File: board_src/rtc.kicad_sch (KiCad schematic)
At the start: 8 parts, among them IC1 PCF8563TS_4,118, J9 Conn_01x02_Pin, Y2 Crystal

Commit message: wersja dodane arkusze hierarchiczne
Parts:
- removed BT1: Battery, symbol Device:Battery
- added BT2: 502-3, 5023, symbol 502-3:502-3
- added R17, R18: 10k, Resistor_SMD:R_0201_0603Metric, symbol Device:R
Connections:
- net +3.3V is gone; now on net 3,3V: IC1.8 (VDD)
- net SCL: now also R17.1
- net SDA: now also R18.1
- net at D13.2 (A): now also BT2.2 (+)
- net 3,3V: now reaches D12.2 (A)
- net 3,3V: now also R17.2, R18.2
- net GND renamed gnd
- net gnd: now also BT2.1 (-)
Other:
- note removed: "Jakich elementów brakuje?"
- moved on the sheet: C1, C2, D12, D13, IC1, J9, Y2

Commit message: wersja dodane arkusze hierarchiczne
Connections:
- net 3,3V renamed +3.3V
- net gnd renamed GND
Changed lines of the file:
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@@
-	(wire
-		(pts
-			(xy 162.56 127) (xy 160.02 127)
-		)
-		(stroke
-			(width 0)
-			(type default)
-		)
-	)
 	(wire
 		(pts
@@
 		)
 	)
-	(global_label "3,3V"
-		(shape input)
-		(at 242.57 81.28 0)
-		(fields_autoplaced yes)
-		(effects
-			(font
-				(size 1.27 1.27)
-			)
-			(justify left)
-		)
-		(property "Intersheetrefs" "${INTERSHEET_REFS}"
-			(at 249.6676 81.28 0)
-			(effects
-				(font
-					(size 1.27 1.27)
-				)
-				(justify left)
-				(hide yes)
-			)
-		)
-	)
-	(global_label "3,3V"
-		(shape input)
-		(at 114.3 59.69 0)
-		(fields_autoplaced yes)
-		(effects
-			(font
-				(size 1.27 1.27)
-			)
-			(justify left)
-		)
-		(property "Intersheetrefs" "${INTERSHEET_REFS}"
-			(at 121.3976 59.69 0)
-			(effects
-				(font
-					(size 1.27 1.27)
-				)
-				(justify left)
-				(hide yes)
-			)
-		)
-	)
-	(global_label "gnd"
-		(shape input)
-		(at 160.02 127 180)
-		(fields_autoplaced yes)
-		(effects
-			(font
-				(size 1.27 1.27)
-			)
-			(justify right)
-		)
-		(property "Intersheetrefs" "${INTERSHEET_REFS}"
-			(at 153.5878 127 0)
-			(effects
-				(font
-					(size 1.27 1.27)
-				)
-				(justify right)
-				(hide yes)
-			)
-		)
-	)
 	(symbol
 		(lib_id "Device:R")
@@
 	)
 	(symbol
+		(lib_id "power:GND")
+		(at 162.56 127 0)
+		(unit 1)
+		(exclude_from_sim no)
+		(in_bom yes)
+		(on_board yes)
+		(dnp no)
+		(fields_autoplaced yes)
+		(property "Reference" "#PWR018"
+			(at 162.56 133.35 0)
+			(effects
+				(font
+					(size 1.27 1.27)
+				)
+				(hide yes)
+			)
+		)
+		(property "Value" "GND"
+			(at 162.56 132.08 0)
+			(effects
+				(font
+					(size 1.27 1.27)
+				)
+			)
+		)
+		(property "Footprint" ""
+			(at 162.56 127 0)
+			(effects
+				(font
+					(size 1.27 1.27)
+				)
+				(hide yes)
+			)
+		)
+		(property "Datasheet" ""
+			(at 162.56 127 0)
+			(effects
+				(font
+					(size 1.27 1.27)
+				)
+				(hide yes)
+			)
+		)
+		(property "Description" "Power symbol creates a global label with name \"GND\" , ground"
+			(at 162.56 127 0)
+			(effects
+				(font
+					(size 1.27 1.27)
+				)
+				(hide yes)
+			)
+		)
+		(pin "1"
+		)
+		(instances
+			(project ""
+				(path "/772e9f49-cfcf-4cf6-843d-0684684f2d4b/aeaae9df-f534-49c0-80c6-5a1da97c1479"
+					(reference "#PWR018")
+					(unit 1)
+				)
+			)
+		)
+	)
+	(symbol
 		(lib_id "Device:C")
 		(at 127 80.01 180)
@@
 					(unit 1)
 				)
+			)
+		)
+	)
+	(symbol
+		(lib_id "power:+3.3V")
+		(at 114.3 59.69 270)
+		(unit 1)
+		(exclude_from_sim no)
+		(in_bom yes)
+		(on_board yes)
+		(dnp no)
+		(fields_autoplaced yes)
+		(property "Reference" "#PWR019"
+			(at 110.49 59.69 0)
+			(effects
+				(font
+					(size 1.27 1.27)
+				)
+				(hide yes)
+			)
+		)
+		(property "Value" "+3.3V"
+			(at 118.11 59.6899 90)
+			(effects
+				(font
+					(size 1.27 1.27)
+				)
+				(justify left)
+			)
+		)
+		(property "Footprint" ""
+			(at 114.3 59.69 0)
+			(effects
+				(font
+					(size 1.27 1.27)
+				)
+				(hide yes)
+			)
+		)
+		(property "Datasheet" ""
+			(at 114.3 59.69 0)
+			(effects
+				(font
+					(size 1.27 1.27)
+				)
+				(hide yes)
+			)
+		)
+		(property "Description" "Power symbol creates a global label with name \"+3.3V\""
+			(at 114.3 59.69 0)
+			(effects
+				(font
+					(size 1.27 1.27)
+				)
+				(hide yes)
+			)
+		)
+		(pin "1"
+		)
+		(instances
+			(project "board"
+				(path "/772e9f49-cfcf-4cf6-843d-0684684f2d4b/aeaae9df-f534-49c0-80c6-5a1da97c1479"
+					(reference "#PWR019")
+					(unit 1)
+				)
+			)
+		)
+	)
+	(symbol
+		(lib_id "power:+3.3V")
+		(at 242.57 81.28 270)
+		(unit 1)
+		(exclude_from_sim no)
+		(in_bom yes)
+		(on_board yes)
+		(dnp no)
+		(fields_autoplaced yes)
+		(property "Reference" "#PWR011"
+			(at 238.76 81.28 0)
+			(effects
+				(font
+					(size 1.27 1.27)
+				)
+				(hide yes)
+			)
+		)
+		(property "Value" "+3.3V"
+			(at 246.38 81.2799 90)
+			(effects
+				(font
+					(size 1.27 1.27)
+				)
+				(justify left)
+			)
+		)
+		(property "Footprint" ""
+			(at 242.57 81.28 0)
+			(effects
+				(font
+					(size 1.27 1.27)
+				)
+				(hide yes)
+			)
+		)
+		(property "Datasheet" ""
+			(at 242.57 81.28 0)
+			(effects
+				(font
+					(size 1.27 1.27)
+				)
+				(hide yes)
+			)
+		)
+		(property "Description" "Power symbol creates a global label with name \"+3.3V\""
+			(at 242.57 81.28 0)
+			(effects
+				(font
+					(size 1.27 1.27)
+				)
+				(hide yes)
+			)
+		)
+		(pin "1"
+		)
+		(instances
+			(project "board"
+				(path "/772e9f49-cfcf-4cf6-843d-0684684f2d4b/aeaae9df-f534-49c0-80c6-5a1da97c1479"
+					(reference "#PWR011")
+					(unit 1)
+				)

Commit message: wersja uzupelnione footprinty
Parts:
- BT2: footprint 5023 -> footprints:podstawka_bateria
- IC1: footprint SOP65P490X110-8N -> footprints:SOP65P490X110-8N
- J9: footprint (none) -> Connector_PinHeader_2.54mm:PinHeader_1x02_P2.54mm_Vertical
- Y2: footprint (none) -> Crystal:Crystal_HC35-U
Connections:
- net SCL: no longer names the net of IC1.6 (SCL), R17.1
- net SDA: no longer names the net of IC1.5 (SDA), R18.1
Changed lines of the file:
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@@
-		)
-	)
-	(label "SDA"
-		(at 220.98 82.55 0)
-		(effects
-			(font
-				(size 1.27 1.27)
-			)
-			(justify left bottom)
-		)
-	)
-	(label "SCL"
-		(at 220.98 80.01 0)
-		(effects
-			(font
-				(size 1.27 1.27)
-			)
-			(justify left bottom)
 		)
 	)
@@
 			)
 		)
-		(property "Footprint" "SOP65P490X110-8N"
+		(property "Footprint" "footprints:SOP65P490X110-8N"
 			(at 213.36 169.85 0)
 			(effects
@@
 			)
 		)
-		(property "Footprint" ""
+		(property "Footprint" "Connector_PinHeader_2.54mm:PinHeader_1x02_P2.54mm_Vertical"
 			(at 204.47 53.34 0)
 			(effects
@@
 			)
 		)
-		(property "Footprint" "5023"
+		(property "Footprint" "footprints:podstawka_bateria"
 			(at 88.9 -6.02 0)
 			(effects
@@
 			)
 		)
-		(property "Footprint" ""
+		(property "Footprint" "Crystal:Crystal_HC35-U"
 			(at 176.53 77.47 0)
 			(effects

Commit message: wersja 3d
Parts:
- Y2: footprint Crystal:Crystal_HC35-U -> Crystal:Crystal_AT310_D3.0mm_L10.0mm_Horizontal
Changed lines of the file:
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@@
 			)
 		)
-		(property "Footprint" "Crystal:Crystal_HC35-U"
+		(property "Footprint" "Crystal:Crystal_AT310_D3.0mm_L10.0mm_Horizontal"
 			(at 176.53 77.47 0)
 			(effects

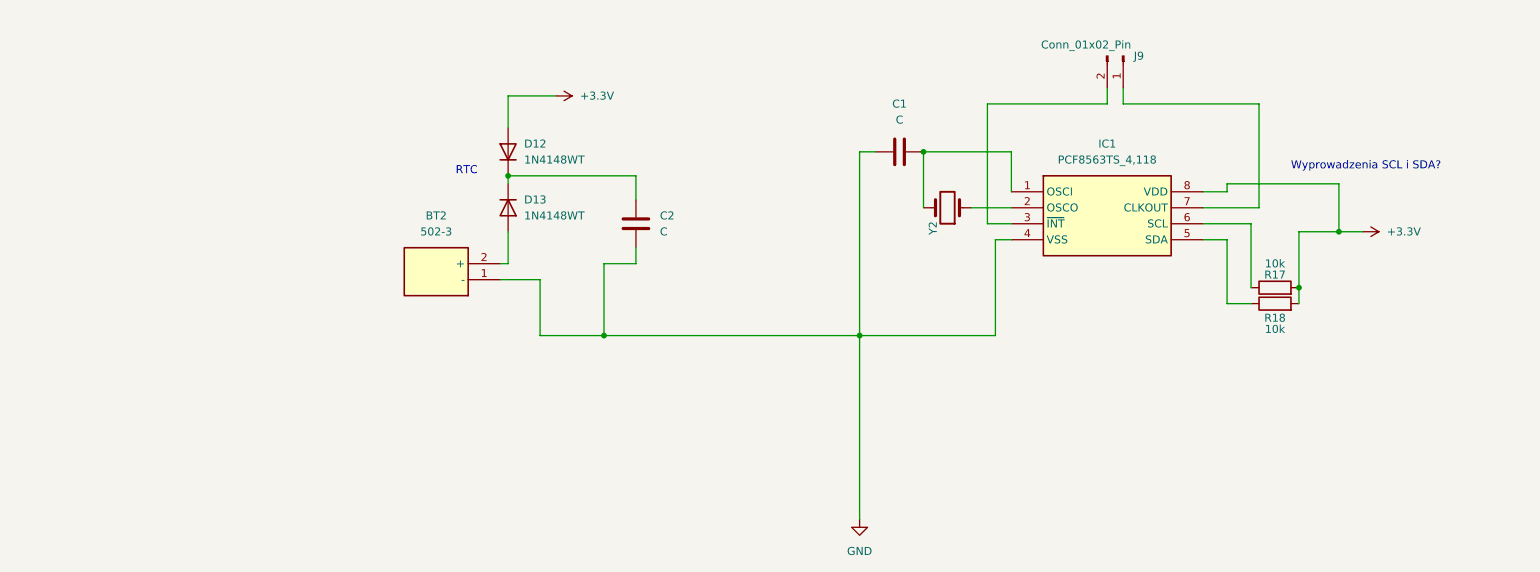
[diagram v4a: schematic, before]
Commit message: wersja z wyswietlaczem LCD
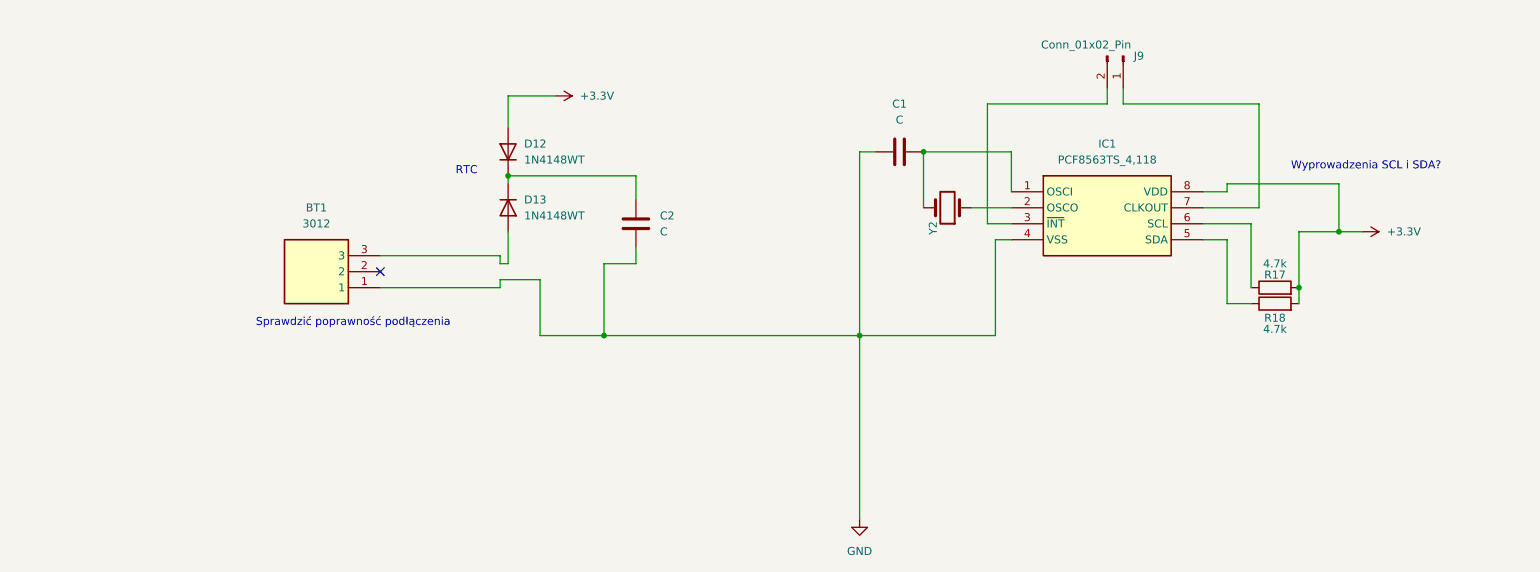
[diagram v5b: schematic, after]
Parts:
- removed BT2: 502-3, footprints:podstawka_bateria, symbol 502-3:502-3
- added BT1: 3012, footprints:3012, symbol 3012:3012
- R17, R18: value 10k -> 4.7k
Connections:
- net GND: now also BT1.1
- net at D13.2 (A): now also BT1.3
- no-connect marks 0 -> 1
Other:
- note added: "Sprawdzić poprawność podłączenia"
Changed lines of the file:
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@@
+		)
+	)
+	(text "Sprawdzić poprawność podłączenia"
+		(exclude_from_sim no)
+		(at 82.042 95.758 0)
+		(effects
+			(font
+				(size 1.27 1.27)
+			)
 		)
 	)
@@
 		(color 0 0 0 0)
 	)
+	(no_connect
+		(at 86.36 87.63)
+	)
 	(wire
 		(pts
@@
 	(wire
 		(pts
+			(xy 105.41 90.17) (xy 105.41 88.9)
+		)
+		(stroke
+			(width 0)
+			(type default)
+		)
+	)
+	(wire
+		(pts
 			(xy 184.15 82.55) (xy 184.15 97.79)
 		)
@@
 	(wire
 		(pts
+			(xy 86.36 85.09) (xy 105.41 85.09)
+		)
+		(stroke
+			(width 0)
+			(type default)
+		)
+	)
+	(wire
+		(pts
 			(xy 226.06 60.96) (xy 204.47 60.96)
 		)
@@
 	(wire
 		(pts
+			(xy 86.36 90.17) (xy 105.41 90.17)
+		)
+		(stroke
+			(width 0)
+			(type default)
+		)
+	)
+	(wire
+		(pts
 			(xy 220.98 74.93) (xy 220.98 73.66)
 		)
@@
 		(pts
 			(xy 232.41 90.17) (xy 232.41 92.71)
+		)
+		(stroke
+			(width 0)
+			(type default)
+		)
+	)
+	(wire
+		(pts
+			(xy 105.41 85.09) (xy 105.41 86.36)
 		)
 		(stroke
@@
 			)
 		)
-		(property "Value" "10k"
+		(property "Value" "4.7k"
 			(at 228.6 96.774 90)
 			(effects
@@
 			)
 		)
-		(property "Value" "10k"
+		(property "Value" "4.7k"
 			(at 228.6 86.36 90)
 			(effects
@@
 	)
 	(symbol
-		(lib_id "502-3:502-3")
-		(at 105.41 88.9 180)
+		(lib_id "3012:3012")
+		(at 86.36 90.17 180)
 		(unit 1)
 		(exclude_from_sim no)
@@
 		(dnp no)
 		(fields_autoplaced yes)
-		(property "Reference" "BT2"
-			(at 95.25 78.74 0)
-			(effects
-				(font
-					(size 1.27 1.27)
-				)
-			)
-		)
-		(property "Value" "502-3"
-			(at 95.25 81.28 0)
-			(effects
-				(font
-					(size 1.27 1.27)
-				)
-			)
-		)
-		(property "Footprint" "footprints:podstawka_bateria"
-			(at 88.9 -6.02 0)
+		(property "Reference" "BT1"
+			(at 76.2 77.47 0)
+			(effects
+				(font
+					(size 1.27 1.27)
+				)
+			)
+		)
+		(property "Value" "3012"
+			(at 76.2 80.01 0)
+			(effects
+				(font
+					(size 1.27 1.27)
+				)
+			)
+		)
+		(property "Footprint" "footprints:3012"
+			(at 69.85 -4.75 0)
 			(effects
 				(font
@@
 			)
 		)
-		(property "Datasheet" "http://www.keyelco.com/product-pdf.cfm?p=4032"
-			(at 88.9 -106.02 0)
+		(property "Datasheet" ""
+			(at 69.85 -104.75 0)
 			(effects
 				(font
@@
 			)
 		)
-		(property "Description" "Coin Cell Battery Holders 16mm Coin cell hldr .635x.505x.060"
-			(at 105.41 88.9 0)
-			(effects
-				(font
-					(size 1.27 1.27)
-				)
-				(hide yes)
-			)
-		)
-		(property "Height" "8.76"
-			(at 88.9 -306.02 0)
+		(property "Description" "BATTERY SOCKET Keystone PCB Mount Battery Contact for 1 (Coin Cell), Top Spring Arm Contact, 16mm Cell Diameter"
+			(at 86.36 90.17 0)
+			(effects
+				(font
+					(size 1.27 1.27)
+				)
+				(hide yes)
+			)
+		)
+		(property "Height" ""
+			(at 69.85 -304.75 0)
 			(effects
 				(font
@@
 		)
 		(property "TME Electronic Components Part Number" ""
-			(at 88.9 -406.02 0)
+			(at 69.85 -404.75 0)
 			(effects
 				(font
@@
 		)
 		(property "TME Electronic Components Price/Stock" ""
-			(at 88.9 -506.02 0)
+			(at 69.85 -504.75 0)
 			(effects
 				(font
@@
 		)
 		(property "Manufacturer_Name" "Keystone Electronics"
-			(at 88.9 -606.02 0)
+			(at 69.85 -604.75 0)
 			(effects
 				(font
@@
 			)
 		)
-		(property "Manufacturer_Part_Number" "502-3"
-			(at 88.9 -706.02 0)
+		(property "Manufacturer_Part_Number" "3012"
+			(at 69.85 -704.75 0)
 			(effects
 				(font
@@
 		)
 		(pin "2"
+		)
+		(pin "3"
 		)
 		(pin "1"
@@
 			(project ""
 				(path "/772e9f49-cfcf-4cf6-843d-0684684f2d4b/aeaae9df-f534-49c0-80c6-5a1da97c1479"
-					(reference "BT2")
+					(reference "BT1")
 					(unit 1)
 				)

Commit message: wersja z FT232RN
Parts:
- removed BT1: 3012, footprints:3012, symbol 3012:3012
- removed C2: C, Capacitor_SMD:C_0201_0603Metric, symbol Device:C
- removed D12, D13: 1N4148WT, Diode_SMD:D_SOD-523, symbol Diode:1N4148WT
- removed R17, R18: 4.7k, Resistor_SMD:R_0201_0603Metric, symbol Device:R
- added J10: Conn_01x02_Pin, Connector_PinHeader_2.54mm:PinHeader_1x02_P2.54mm_Vertical, symbol Connector:Conn_01x02_Pin
- added R43, R44: 4.7k, Resistor_SMD:R_1206_3216Metric, symbol Device:R
- C1: footprint Capacitor_SMD:C_0201_0603Metric -> Capacitor_SMD:C_1206_3216Metric
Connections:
- net +3.3V: now also R43.2, R44.2
- net at IC1.5 (SDA): now also J10.1 (Pin_1), R44.1
- net INT: now reaches IC1.3 (~{INT}), J9.2 (Pin_2)
- net at IC1.6 (SCL): now also J10.2 (Pin_2), R43.1
- net CLKOUT: now reaches IC1.7 (CLKOUT), J9.1 (Pin_1)
- no-connect marks 1 -> 0
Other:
- note removed: "RTC"
- note removed: "Sprawdzić poprawność podłączenia"
- note removed: "Wyprowadzenia SCL i SDA?"
- moved on the sheet: C1, J9, Y2

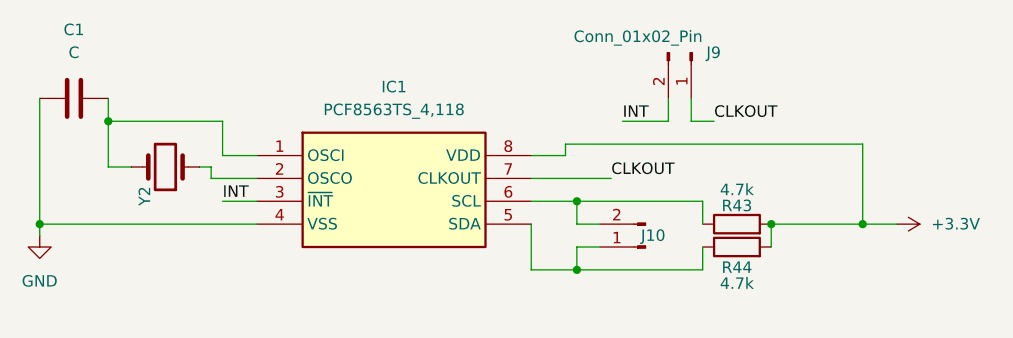
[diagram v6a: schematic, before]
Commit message: Wersja ze sciezkami miedzianymi
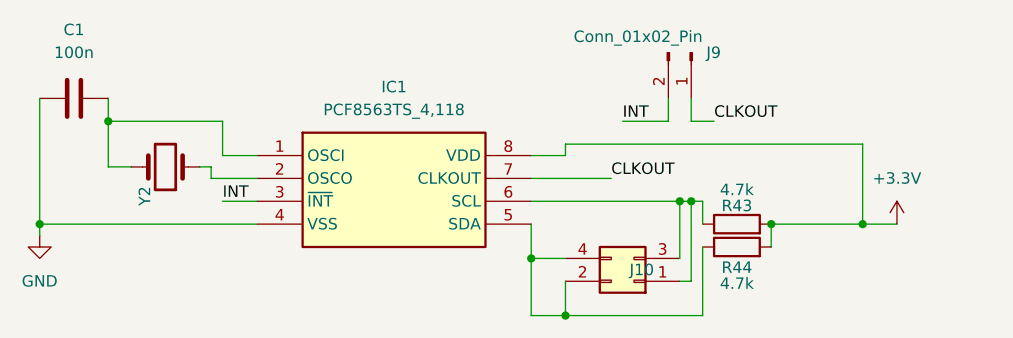
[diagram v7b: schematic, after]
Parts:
- C1: value C -> 100n; footprint Capacitor_SMD:C_1206_3216Metric -> Capacitor_SMD:C_0603_1608Metric
- J10: footprint Connector_PinHeader_2.54mm:PinHeader_1x02_P2.54mm_Vertical -> Connector_PinHeader_2.54mm:PinHeader_2x02_P2.54mm_Vertical; symbol Connector:Conn_01x02_Pin -> Connector_Generic:Conn_02x02_Odd_Even
- R43, R44: footprint Resistor_SMD:R_1206_3216Metric -> Resistor_SMD:R_0603_1608Metric
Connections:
- net at IC1.6 (SCL), R43.1: now also J10.1 (Pin_1), J10.3 (Pin_3); no longer J10.2 (Pin_2)
- net at IC1.5 (SDA), R44.1: now also J10.2 (Pin_2), J10.4 (Pin_4); no longer J10.1 (Pin_1)
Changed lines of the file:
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@@
 	(paper "A4")
-	(junction
-		(at 222.25 80.01)
-		(diameter 0)
-		(color 0 0 0 0)
-	)
 	(junction
 		(at 170.18 71.12)
@@
 	)
 	(junction
+		(at 217.17 86.36)
+		(diameter 0)
+		(color 0 0 0 0)
+	)
+	(junction
 		(at 162.56 82.55)
+		(diameter 0)
+		(color 0 0 0 0)
+	)
+	(junction
+		(at 220.98 92.71)
+		(diameter 0)
+		(color 0 0 0 0)
+	)
+	(junction
+		(at 234.95 80.01)
 		(diameter 0)
 		(color 0 0 0 0)
@@
 	)
 	(junction
-		(at 222.25 87.63)
+		(at 233.68 80.01)
 		(diameter 0)
 		(color 0 0 0 0)
@@
 	(wire
 		(pts
+			(xy 217.17 92.71) (xy 220.98 92.71)
+		)
+		(stroke
+			(width 0)
+			(type default)
+		)
+	)
+	(wire
+		(pts
 			(xy 232.41 71.12) (xy 227.33 71.12)
 		)
@@
 	(wire
 		(pts
-			(xy 222.25 80.01) (xy 236.22 80.01)
-		)
-		(stroke
-			(width 0)
-			(type default)
-		)
-	)
-	(wire
-		(pts
-			(xy 236.22 87.63) (xy 236.22 85.09)
-		)
-		(stroke
-			(width 0)
-			(type default)
-		)
-	)
-	(wire
-		(pts
-			(xy 217.17 80.01) (xy 222.25 80.01)
-		)
-		(stroke
-			(width 0)
-			(type default)
-		)
-	)
-	(wire
-		(pts
-			(xy 224.79 82.55) (xy 222.25 82.55)
+			(xy 234.95 88.9) (xy 234.95 80.01)
+		)
+		(stroke
+			(width 0)
+			(type default)
+		)
+	)
+	(wire
+		(pts
+			(xy 236.22 92.71) (xy 236.22 85.09)
 		)
 		(stroke
@@
 	(wire
 		(pts
+			(xy 217.17 80.01) (xy 233.68 80.01)
+		)
+		(stroke
+			(width 0)
+			(type default)
+		)
+	)
+	(wire
+		(pts
+			(xy 233.68 88.9) (xy 234.95 88.9)
+		)
+		(stroke
+			(width 0)
+			(type default)
+		)
+	)
+	(wire
+		(pts
+			(xy 233.68 80.01) (xy 233.68 86.36)
+		)
+		(stroke
+			(width 0)
+			(type default)
+		)
+	)
+	(wire
+		(pts
 			(xy 162.56 82.55) (xy 162.56 83.82)
 		)
@@
 	(wire
 		(pts
-			(xy 217.17 87.63) (xy 222.25 87.63)
+			(xy 234.95 80.01) (xy 236.22 80.01)
 		)
 		(stroke
@@
 	(wire
 		(pts
+			(xy 220.98 92.71) (xy 236.22 92.71)
+		)
+		(stroke
+			(width 0)
+			(type default)
+		)
+	)
+	(wire
+		(pts
+			(xy 220.98 88.9) (xy 220.98 92.71)
+		)
+		(stroke
+			(width 0)
+			(type default)
+		)
+	)
+	(wire
+		(pts
 			(xy 182.88 74.93) (xy 186.69 74.93)
 		)
@@
 	(wire
 		(pts
-			(xy 222.25 85.09) (xy 222.25 87.63)
-		)
-		(stroke
-			(width 0)
-			(type default)
-		)
-	)
-	(wire
-		(pts
-			(xy 224.79 85.09) (xy 222.25 85.09)
-		)
-		(stroke
-			(width 0)
-			(type default)
-		)
-	)
-	(wire
-		(pts
-			(xy 222.25 87.63) (xy 236.22 87.63)
+			(xy 217.17 86.36) (xy 217.17 92.71)
+		)
+		(stroke
+			(width 0)
+			(type default)
+		)
+	)
+	(wire
+		(pts
+			(xy 217.17 86.36) (xy 220.98 86.36)
+		)
+		(stroke
+			(width 0)
+			(type default)
+		)
+	)
+	(wire
+		(pts
+			(xy 233.68 80.01) (xy 234.95 80.01)
 		)
 		(stroke
@@
 	(wire
 		(pts
-			(xy 222.25 80.01) (xy 222.25 82.55)
-		)
-		(stroke
-			(width 0)
-			(type default)
-		)
-	)
-	(wire
-		(pts
 			(xy 170.18 76.2) (xy 170.18 71.12)
 		)
@@
 	(wire
 		(pts
-			(xy 217.17 82.55) (xy 217.17 87.63)
+			(xy 217.17 82.55) (xy 217.17 86.36)
 		)
 		(stroke
@@
 			)
 		)
-		(property "Footprint" "Resistor_SMD:R_1206_3216Metric"
+		(property "Footprint" "Resistor_SMD:R_0603_1608Metric"
 			(at 240.03 84.328 90)
 			(effects
@@
 			)
 		)
-		(property "Footprint" "Resistor_SMD:R_1206_3216Metric"
+		(property "Footprint" "Resistor_SMD:R_0603_1608Metric"
 			(at 240.03 86.868 90)
 			(effects
@@
 			)
 		)
-		(property "Value" "C"
+		(property "Value" "100n"
 			(at 166.37 63.5 90)
 			(effects
@@
 			)
 		)
-		(property "Footprint" "Capacitor_SMD:C_1206_3216Metric"
+		(property "Footprint" "Capacitor_SMD:C_0603_1608Metric"
 			(at 170.18 67.6148 0)
 			(effects
@@
 	)
 	(symbol
-		(lib_id "Connector:Conn_01x02_Pin")
-		(at 229.87 85.09 180)
+		(lib_id "Connector_Generic:Conn_02x02_Odd_Even")
+		(at 228.6 88.9 180)
 		(unit 1)
 		(exclude_from_sim no)
@@
 		(dnp no)
 		(property "Reference" "J10"
-			(at 229.362 83.82 0)
+			(at 228.092 87.63 0)
 			(effects
 				(font
@@
 		)
 		(property "Value" "Conn_01x02_Pin"
-			(at 233.934 82.296 0)
+			(at 232.664 86.106 0)
 			(effects
 				(font
@@
 			)
 		)
-		(property "Footprint" "Connector_PinHeader_2.54mm:PinHeader_1x02_P2.54mm_Vertical"
-			(at 229.87 85.09 0)
+		(property "Footprint" "Connector_PinHeader_2.54mm:PinHeader_2x02_P2.54mm_Vertical"
+			(at 228.6 88.9 0)
 			(effects
 				(font
@@
 		)
 		(property "Datasheet" "~"
-			(at 229.87 85.09 0)
-			(effects
-				(font
-					(size 1.27 1.27)
-				)
-				(hide yes)
-			)
-		)
-		(property "Description" "Generic connector, single row, 01x02, script generated"
-			(at 229.87 85.09 0)
+			(at 228.6 88.9 0)
+			(effects
+				(font
+					(size 1.27 1.27)
+				)
+				(hide yes)
+			)
+		)
+		(property "Description" "Generic connector, double row, 02x02, odd/even pin numbering scheme (row 1 odd numbers, row 2 even numbers), script generated (kicad-library-utils/schlib/autogen/connector/)"
+			(at 228.6 88.9 0)
 			(effects
 				(font
@@
 		)
 		(pin "2"
+		)
+		(pin "3"
+		)
+		(pin "4"
 		)
 		(instances
@@
 	(symbol
 		(lib_id "power:+3.3V")
-		(at 257.81 82.55 270)
+		(at 257.81 82.55 0)
 		(unit 1)
 		(exclude_from_sim no)
@@
 		(fields_autoplaced yes)
 		(property "Reference" "#PWR011"
-			(at 254 82.55 0)
+			(at 257.81 86.36 0)
 			(effects
 				(font
@@
 		)
 		(property "Value" "+3.3V"
-			(at 261.62 82.5499 90)
-			(effects
-				(font
-					(size 1.27 1.27)
-				)
-				(justify left)
-			)
-		)
+			(at 257.81 77.47 0)
+			(effects
+				(font
+					(size 1.27 1.27)
+				)
+			)
+		)
